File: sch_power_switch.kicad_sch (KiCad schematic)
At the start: 22 parts, among them Q11 BSN20BKR, Q12 BSN20BKR, Q21 BSL307SP, Q22 BSL307SP

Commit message: WIP - Updating analog switch
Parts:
- renumbered C16 to C21, C17 to C22, C18 to C23, C19 to C24, C8 to C31, C9 to C32, C10 to C33, C11 to C34, C12 to C41, C13 to C42, C14 to C43, C15 to C44
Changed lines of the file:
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@@
+	(wire
+		(pts
+			(xy 142.24 129.54) (xy 152.4 129.54)
+		)
+		(stroke
+			(width 0)
+			(type default)
+		)
+	)
 	(wire
 		(pts
@@
 	(wire
 		(pts
-			(xy 142.24 129.54) (xy 152.4 129.54)
-		)
-		(stroke
-			(width 0)
-			(type default)
-		)
-	)
-	(wire
-		(pts
 			(xy 162.56 86.36) (xy 162.56 88.9)
 		)
@@
 	)
 	(label "PWR1"
-		(at 41.91 129.54 0)
+		(at 40.64 129.54 0)
 		(effects
 			(font
@@
 	)
 	(label "PWR2"
-		(at 143.51 129.54 0)
+		(at 142.24 129.54 0)
 		(effects
 			(font
@@
 		)
 	)
-	(hierarchical_label "EN_PWR"
+	(hierarchical_label "EN_PWR[1..2]"
 		(shape input)
 		(at 25.4 111.76 180)
@@
 		)
 	)
-	(hierarchical_label "PWR"
+	(hierarchical_label "PWR[1..2]"
 		(shape output)
 		(at 243.84 25.4 0)
@@
 		(dnp no)
 		(fields_autoplaced yes)
-		(property "Reference" "C16"
+		(property "Reference" "C21"
 			(at 54.61 175.2599 0)
 			(effects
@@
 			(project "pbm_driver4_v2"
 				(path "/04797749-7aaf-42f7-a5f4-0b9aeb0ad7be/ed8a224b-ca38-4f3f-bfc4-14836f79ea5f"
-					(reference "C16")
+					(reference "C21")
 					(unit 1)
 				)
@@
 		(dnp no)
 		(fields_autoplaced yes)
-		(property "Reference" "C14"
+		(property "Reference" "C43"
 			(at 207.01 140.9699 0)
 			(effects
@@
 			(project "pbm_driver4_v2"
 				(path "/04797749-7aaf-42f7-a5f4-0b9aeb0ad7be/ed8a224b-ca38-4f3f-bfc4-14836f79ea5f"
-					(reference "C14")
+					(reference "C43")
 					(unit 1)
 				)
@@
 		(dnp no)
 		(fields_autoplaced yes)
-		(property "Reference" "C11"
+		(property "Reference" "C34"
 			(at 130.81 140.9699 0)
 			(effects
@@
 			(project "pbm_driver4_v2"
 				(path "/04797749-7aaf-42f7-a5f4-0b9aeb0ad7be/ed8a224b-ca38-4f3f-bfc4-14836f79ea5f"
-					(reference "C11")
+					(reference "C34")
 					(unit 1)
 				)
@@
 		(dnp no)
 		(fields_autoplaced yes)
-		(property "Reference" "C17"
+		(property "Reference" "C22"
 			(at 80.01 175.2599 0)
 			(effects
@@
 			(project "pbm_driver4_v2"
 				(path "/04797749-7aaf-42f7-a5f4-0b9aeb0ad7be/ed8a224b-ca38-4f3f-bfc4-14836f79ea5f"
-					(reference "C17")
+					(reference "C22")
 					(unit 1)
 				)
@@
 		(dnp no)
 		(fields_autoplaced yes)
-		(property "Reference" "C18"
+		(property "Reference" "C23"
 			(at 105.41 175.2599 0)
 			(effects
@@
 			(project "pbm_driver4_v2"
 				(path "/04797749-7aaf-42f7-a5f4-0b9aeb0ad7be/ed8a224b-ca38-4f3f-bfc4-14836f79ea5f"
-					(reference "C18")
+					(reference "C23")
 					(unit 1)
 				)
@@
 		(dnp no)
 		(fields_autoplaced yes)
-		(property "Reference" "C13"
+		(property "Reference" "C42"
 			(at 181.61 140.9699 0)
 			(effects
@@
 			(project "pbm_driver4_v2"
 				(path "/04797749-7aaf-42f7-a5f4-0b9aeb0ad7be/ed8a224b-ca38-4f3f-bfc4-14836f79ea5f"
-					(reference "C13")
+					(reference "C42")
 					(unit 1)
 				)
@@
 		(dnp no)
 		(fields_autoplaced yes)
-		(property "Reference" "C12"
+		(property "Reference" "C41"
 			(at 156.21 140.9699 0)
 			(effects
@@
 			(project "pbm_driver4_v2"
 				(path "/04797749-7aaf-42f7-a5f4-0b9aeb0ad7be/ed8a224b-ca38-4f3f-bfc4-14836f79ea5f"
-					(reference "C12")
+					(reference "C41")
 					(unit 1)
 				)
@@
 		(dnp no)
 		(fields_autoplaced yes)
-		(property "Reference" "C10"
+		(property "Reference" "C33"
 			(at 105.41 140.9699 0)
 			(effects
@@
 			(project "pbm_driver4_v2"
 				(path "/04797749-7aaf-42f7-a5f4-0b9aeb0ad7be/ed8a224b-ca38-4f3f-bfc4-14836f79ea5f"
-					(reference "C10")
+					(reference "C33")
 					(unit 1)
 				)
@@
 		(dnp no)
 		(fields_autoplaced yes)
-		(property "Reference" "C8"
+		(property "Reference" "C31"
 			(at 54.61 140.9699 0)
 			(effects
@@
 			(project ""
 				(path "/04797749-7aaf-42f7-a5f4-0b9aeb0ad7be/ed8a224b-ca38-4f3f-bfc4-14836f79ea5f"
-					(reference "C8")
+					(reference "C31")
 					(unit 1)
 				)
@@
 	)
 	(symbol
+		(lib_name "R_0603_10K_1")
 		(lib_id "$Local:R_0603_10K")
 		(at 60.96 82.55 0)
@@
 			)
 		)
-		(property "Description" "RES SMD 10K OHM 0.1% 1/10W 0603"
+		(property "Description" "RES SMD 10K OHM 1% 1/10W 0603"
 			(at 60.96 82.55 0)
 			(effects
@@
 		(dnp no)
 		(fields_autoplaced yes)
-		(property "Reference" "C19"
+		(property "Reference" "C24"
 			(at 130.81 175.2599 0)
 			(effects
@@
 			(project "pbm_driver4_v2"
 				(path "/04797749-7aaf-42f7-a5f4-0b9aeb0ad7be/ed8a224b-ca38-4f3f-bfc4-14836f79ea5f"
-					(reference "C19")
+					(reference "C24")
 					(unit 1)
 				)
@@
 		(dnp no)
 		(fields_autoplaced yes)
-		(property "Reference" "C9"
+		(property "Reference" "C32"
 			(at 80.01 140.9699 0)
 			(effects
@@
 			(project "pbm_driver4_v2"
 				(path "/04797749-7aaf-42f7-a5f4-0b9aeb0ad7be/ed8a224b-ca38-4f3f-bfc4-14836f79ea5f"
-					(reference "C9")
+					(reference "C32")
 					(unit 1)
 				)
@@
 		(dnp no)
 		(fields_autoplaced yes)
-		(property "Reference" "C15"
+		(property "Reference" "C44"
 			(at 232.41 140.9699 0)
 			(effects
@@
 			(project "pbm_driver4_v2"
 				(path "/04797749-7aaf-42f7-a5f4-0b9aeb0ad7be/ed8a224b-ca38-4f3f-bfc4-14836f79ea5f"
-					(reference "C15")
+					(reference "C44")
 					(unit 1)
 				)
@@
 			)
 		)
-		(property "Description" "RES SMD 10K OHM 0.1% 1/10W 0603"
+		(property "Description" "RES SMD 10K OHM 1% 1/10W 0603"
 			(at 162.56 82.55 0)
 			(effects

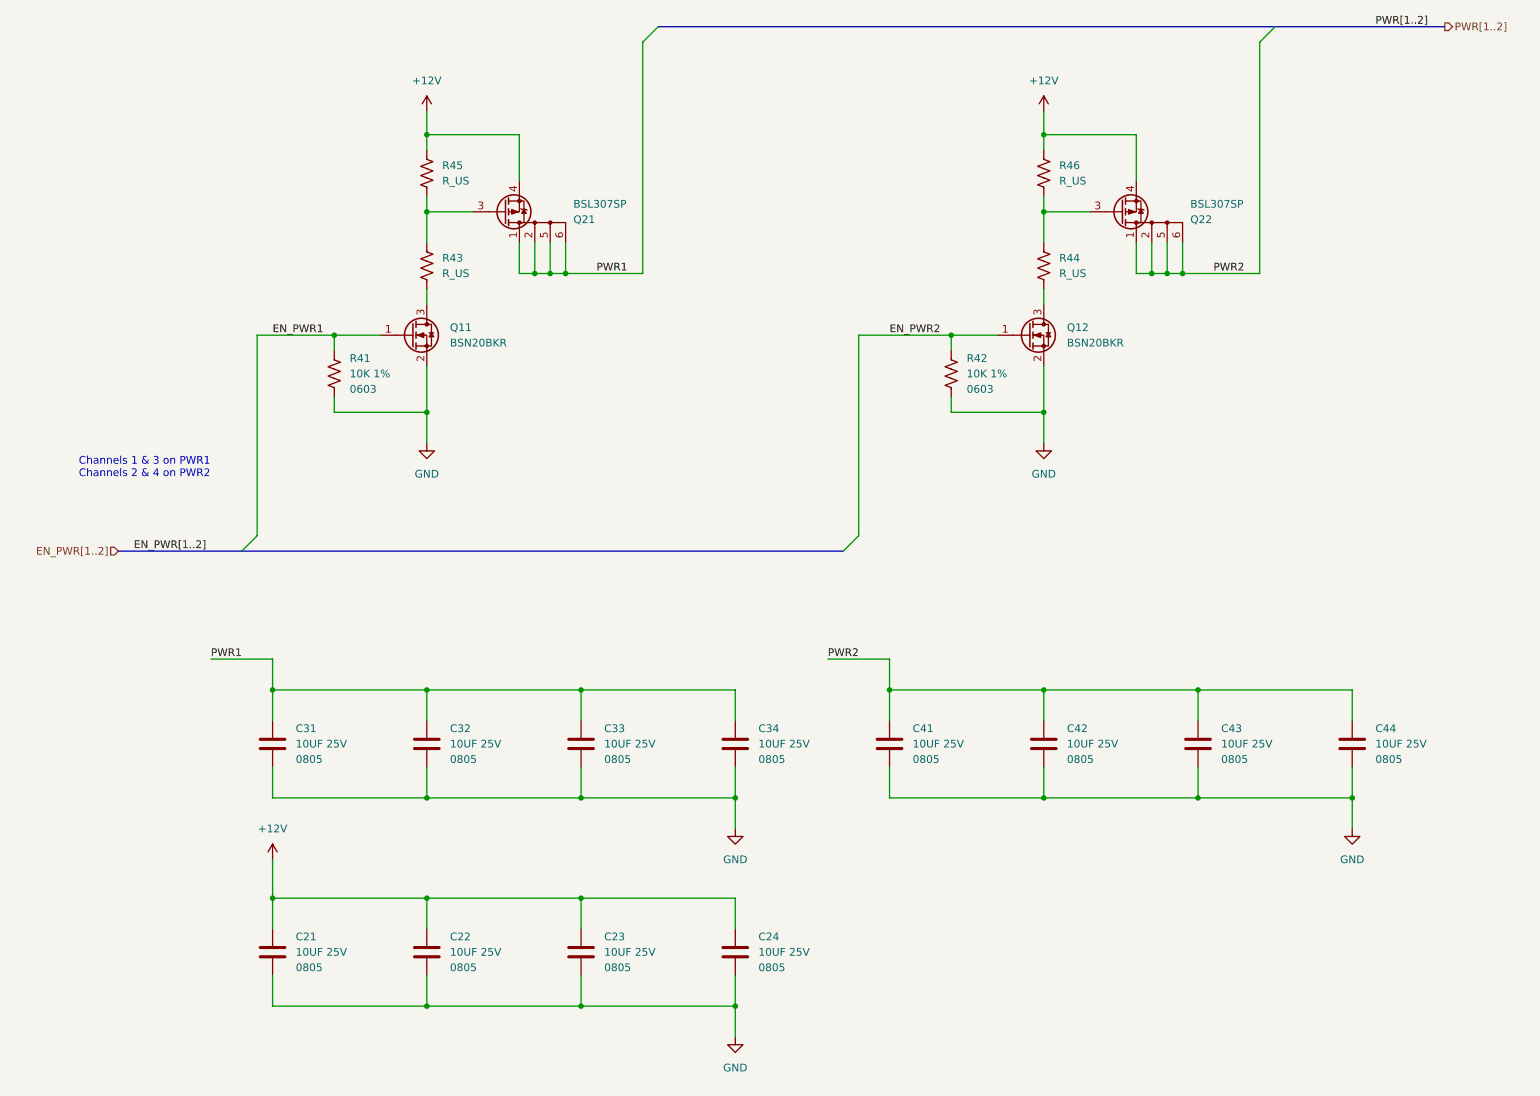
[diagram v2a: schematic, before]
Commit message: Updated 'Size' property to 'Package' on R & C. Cleaned up switch page.
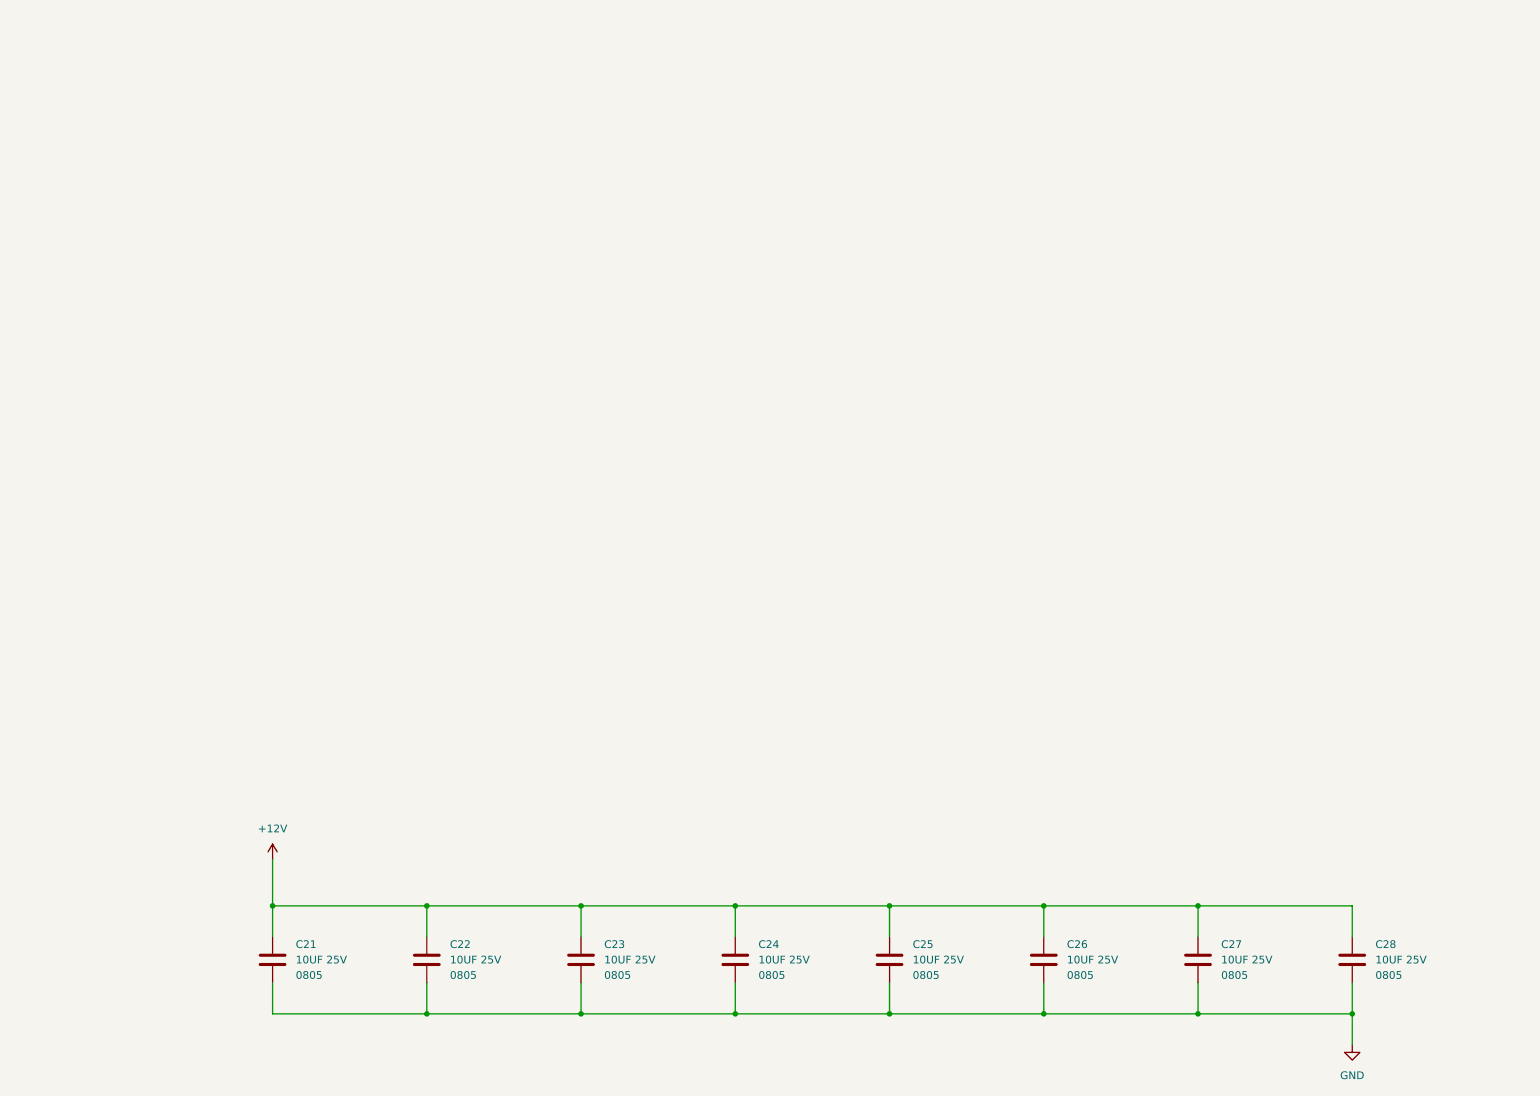
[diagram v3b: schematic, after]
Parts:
- removed C31, C32, C33, C34, C41, C42, C43, C44: 10UF 25V, $Local:C_0805_2012Metric, symbol $Local:C_0805_10UF_25V
- removed Q11, Q12: BSN20BKR, Package_TO_SOT_SMD:SOT-23, symbol $Local:BSN20BKR
- removed Q21, Q22: BSL307SP, Package_SO:TSOP-6_1.65x3.05mm_P0.95mm, symbol $Local:BSL307SP
- removed R41, R42: 10K 1%, $Local:R_0603_1608Metric, symbol $Local:R_0603_10K
- removed R43, R44, R45, R46: R_US, symbol $Local:R_US
- added C25, C26, C27, C28: 10UF 25V, $Local:C_0805_2012Metric, symbol $Local:C_0805_10UF_25V
- C21, C22, C23, C24: Package (none) -> 0805; Size 0805 -> (none)
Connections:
- net +12V: now also C25.1, C26.1, C27.1, C28.1
- net GND: now also C25.2, C26.2, C27.2, C28.2
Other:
- note removed: "Channels 1 & 3 on PWR1 Channels 2 & 4 on PWR2"
- moved on the sheet: C21
